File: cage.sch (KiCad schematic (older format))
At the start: 42 parts

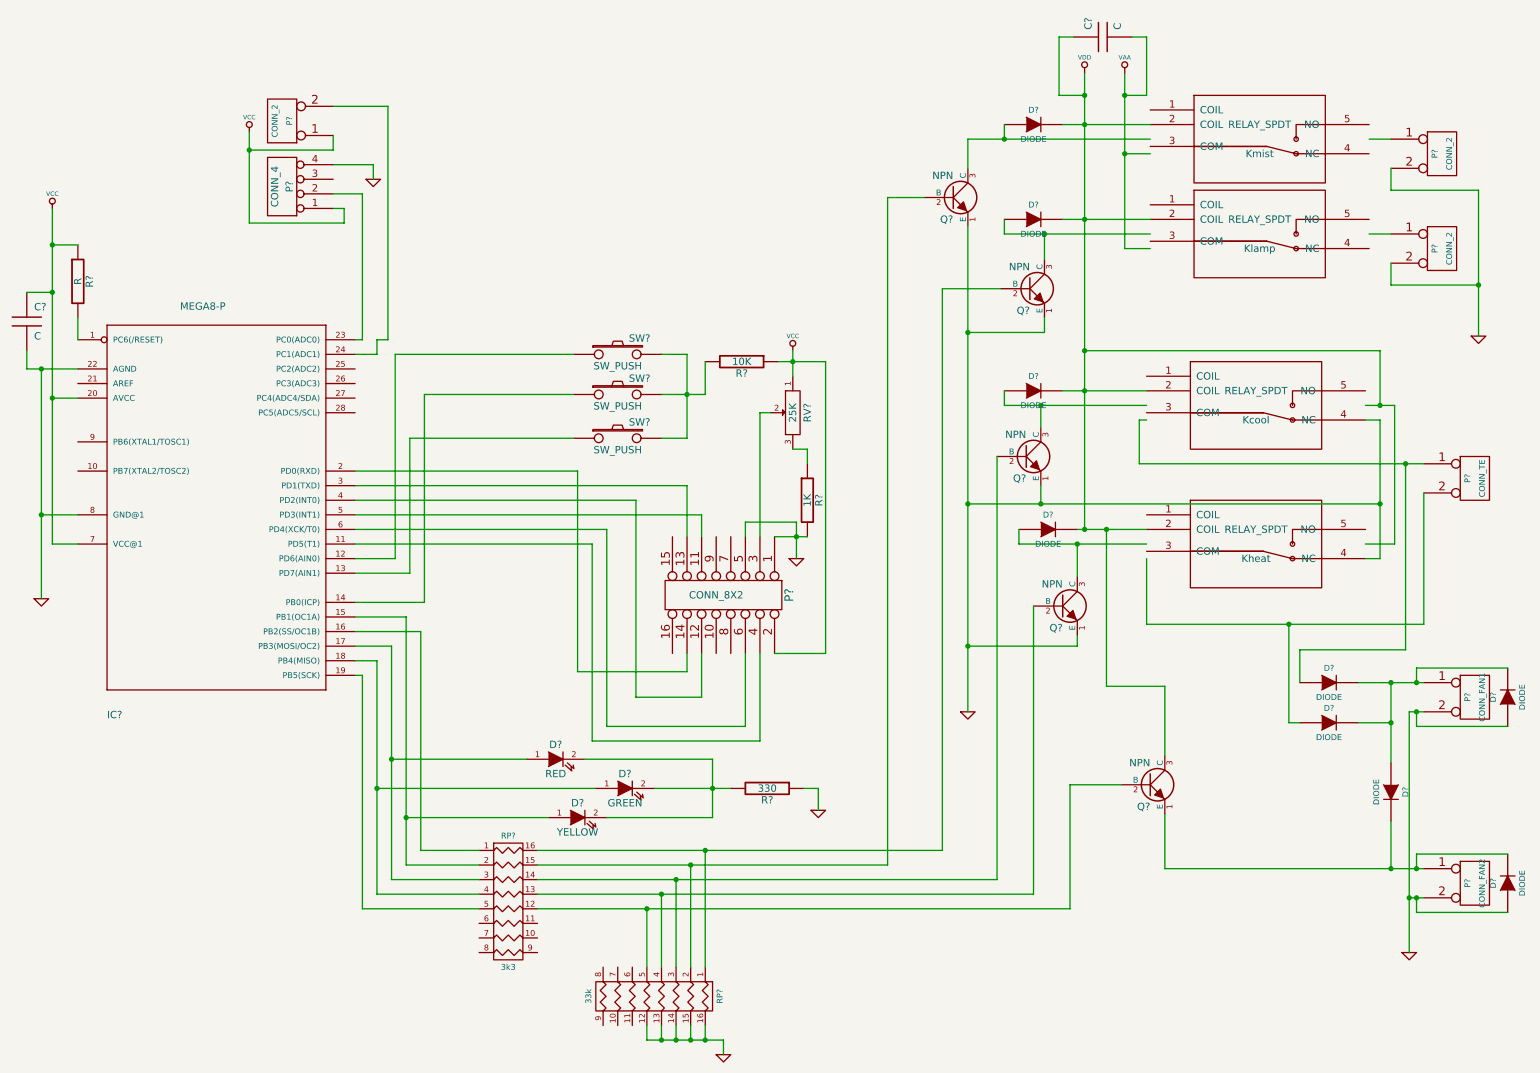
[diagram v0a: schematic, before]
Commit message: changed components to through-hole
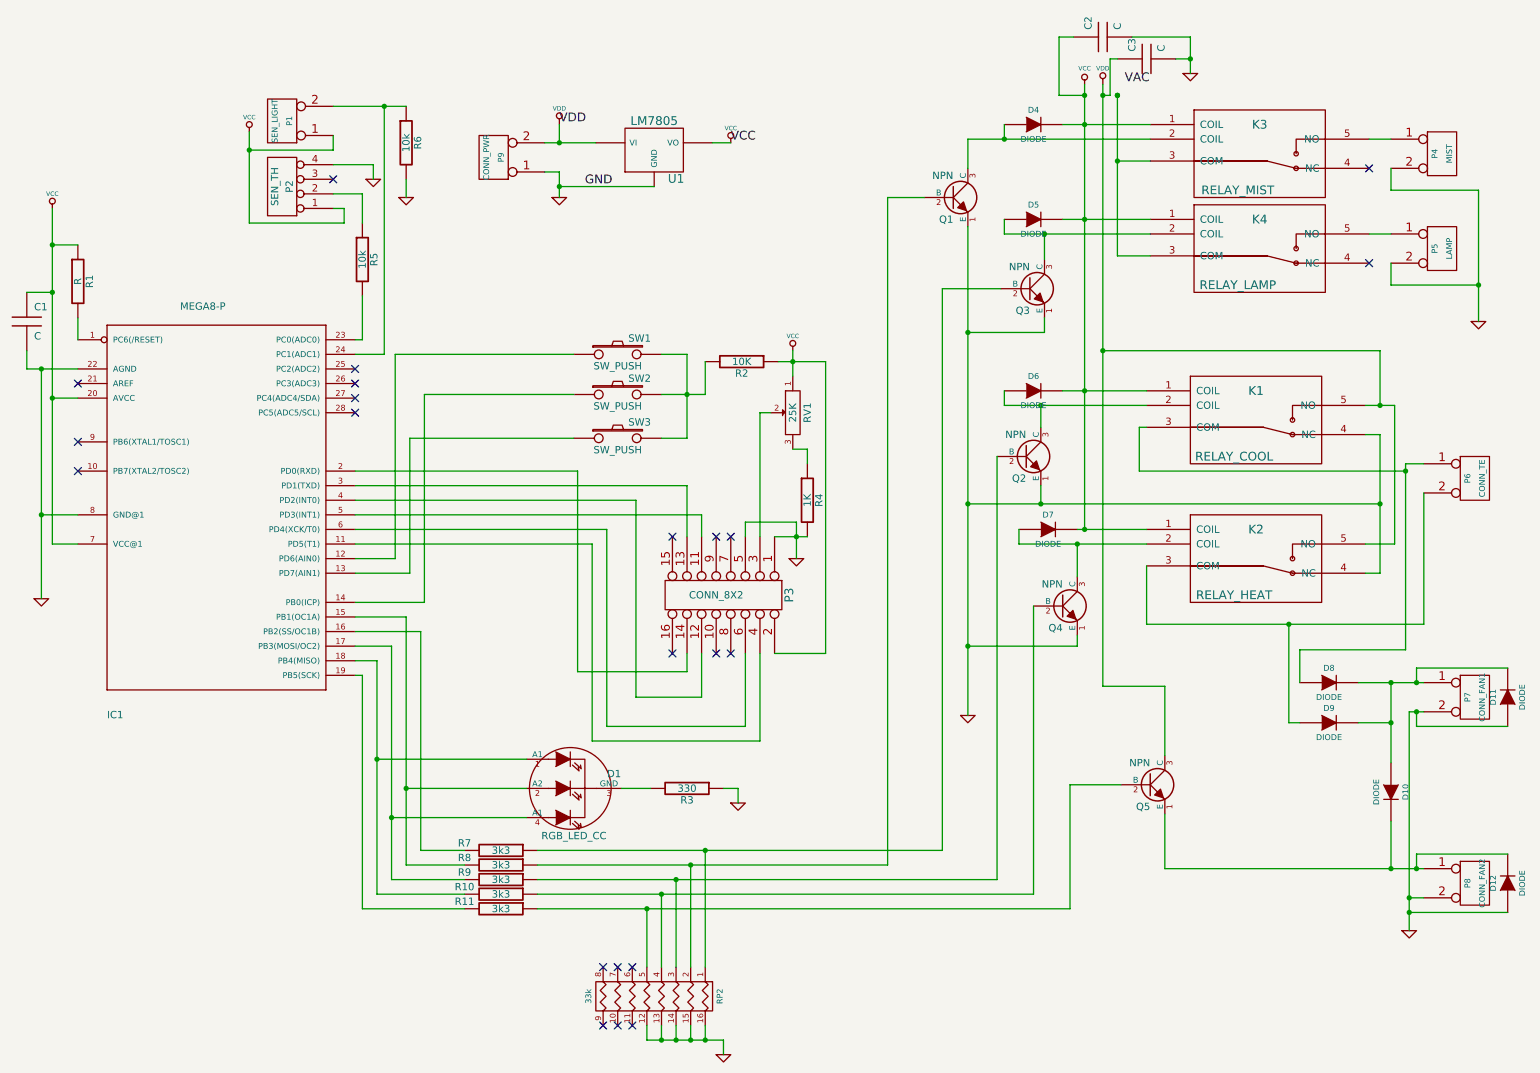
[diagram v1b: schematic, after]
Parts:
- removed D?: YELLOW, symbol LED
- removed D?: GREEN, symbol LED
- removed D?: RED, symbol LED
- removed Kcool, Kheat, Klamp, Kmist: RELAY_SPDT, symbol RELAY_SPDT
- removed RP?: 3k3, symbol R_PACK8
- added C3: C, symbol C
- added D1: RGB_LED_CC, symbol RGB_LED_CC
- added K1: RELAY_COOL, symbol RELAY_SPDT
- added K2: RELAY_HEAT, symbol RELAY_SPDT
- added K3: RELAY_MIST, symbol RELAY_SPDT
- added K4: RELAY_LAMP, symbol RELAY_SPDT
- added P9: CONN_PWR, symbol CONN_2
- added R10, R11, R7, R8, R9: 3k3, symbol R
- added R5, R6: 10k, symbol R
- added U1: LM7805, symbol LM7805
- P1: renamed from P?; value CONN_2 -> SEN_LIGHT
- P2: renamed from P?; value CONN_4 -> SEN_TH
- P4: renamed from P?; value CONN_2 -> MIST
- P5: renamed from P?; value CONN_2 -> LAMP
- gave numbers to parts that had none: 30
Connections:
- net labels added: VAC
- net labels removed: VAA
- wire segments 200 -> 266
- no-connect marks 0 -> 22
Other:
- moved on the sheet: R3
